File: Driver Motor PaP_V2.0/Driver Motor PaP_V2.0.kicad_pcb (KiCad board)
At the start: 2 copper layers, 70 x 60 mm, 31 parts, among them J1 Conn_01x02, J2 Conn_01x02, J3 Conn_01x04, J4 Conn_01x04, J5 Conn_01x01, J6 Conn_01x02, J7 Conn_01x02, J8 Conn_01x01, Q1 BC547, U1 LM358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

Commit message: Finalizado el ruteo. Revisar nuevamente
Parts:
- C4: footprint Capacitor_THT:CP_Radial_D10.0mm_P2.50mm -> Capacitor_THT:CP_Radial_D6.3mm_P2.50mm
- moved J5 21.8 mm to (140.5, 62.8)
- moved J3 18.9 mm to (90.0, 53.8)
- moved JP3 13.9 mm to (125.8, 87.8), turned to 0 degrees
- moved JP1 13.0 mm to (114.0, 87.8), turned to 0 degrees
- moved R2 9.53 mm to (117.0, 71.8), turned to 90 degrees
- moved R1 8.55 mm to (78.8, 76.0), turned to 90 degrees
- moved U3 8.04 mm to (125.8, 76.2), turned to 90 degrees
- moved C3 7.88 mm to (125.8, 64.5), turned to 0 degrees
- moved R3 7.25 mm to (123.0, 81.8), turned to 180 degrees
- moved JP5 5.94 mm to (103.5, 63.8)
- moved U2 5.50 mm to (133.2, 93.8)
- moved JP4 4.67 mm to (106.0, 75.2)
- moved JP2 4.09 mm to (120.0, 87.8)
- moved C2 3.26 mm to (133.5, 82.2), turned to 0 degrees
- moved J1 3.25 mm to (80.5, 89.5)
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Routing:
- net VCC: track 0.06 -> 130.9 mm
- net Net-(A1-Pad10): track 0.00 -> 40.3 mm
- net Net-(JP6-Pad2): track 0.00 -> 35.5 mm
- net Net-(A1-Pad11): track 0.00 -> 33.4 mm
- net Net-(J3-Pad4): track 0.00 -> 22.6 mm
- net Net-(JP2-Pad1): track 0.00 -> 20.9 mm
- net Net-(A1-Pad12): track 0.41 -> 20.3 mm
- net Net-(J4-Pad4): track 0.00 -> 19.0 mm
- net Net-(A1-Pad16): track 0.00 -> 18.0 mm
- net Net-(A1-Pad15): track 0.00 -> 16.1 mm
- net Net-(J4-Pad3): track 0.23 -> 16.3 mm
- net Net-(J5-Pad1): track 0.00 -> 14.6 mm
- net Net-(J4-Pad2): track 0.00 -> 11.7 mm
- net Net-(J3-Pad3): track 0.23 -> 11.9 mm
- net Net-(A1-Pad9): track 0.01 -> 11.0 mm
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- added copper zone on B.Cu, net GND
- added copper zone on F.Cu, net GND
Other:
- board text added: "Ancho de pista : 0,5 mm y 1.2 mm"
- board text added: "Autor: Esp. Ing. Luis Mariano Campos"
- board text added: "Diseño Argentino"
- board text added: "Distancia a borde: 0,5 mm"
- board text added: "Doble Faz"
- board text added: "Driver Motor PaP"
- board text added: "Facultad de Ingeniería - U.B.A."
- board text added: "Fault"
- board text added: "Grillas 0,25 mm"
- board text added: "M0"
- board text added: "M1"
- board text added: "M2"
- board text added: "Margen General: 0,5 mm"
- board text added: "Mínimos:"
- board text added: "PCB espesor: 1,6 mm"
- board text added: "Proyecto Final - CESE 8va Cohorte 2019"
- board text added: "Sherpa - v2.0"
- board text added: "Terminacioń HASL."
- board text added: "Vmotor"
- board text added: "ciaa"
- board text added: "dir"
- board text added: "enable"
- board text added: "gnd"
- board text added: "phase A"
- board text added: "phase B"
- board text added: "st-in"
- board text added: "st-out"
- board text added: "stp"
- board text added: "vcc"

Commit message: PCB FInalizadoy con BOM, realizar una última verificación
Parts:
- moved D1 0.25 mm to (80.2, 81.5)
- moved J1 0.25 mm to (80.8, 89.5)
- moved J3 0.25 mm to (90.0, 54.0)
- moved J4 0.25 mm to (140.8, 70.1)
- moved J6 0.25 mm to (92.0, 105.5)
- moved J7 0.25 mm to (100.3, 105.5)
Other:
- board text added: "ena"
- board text removed: "enable"

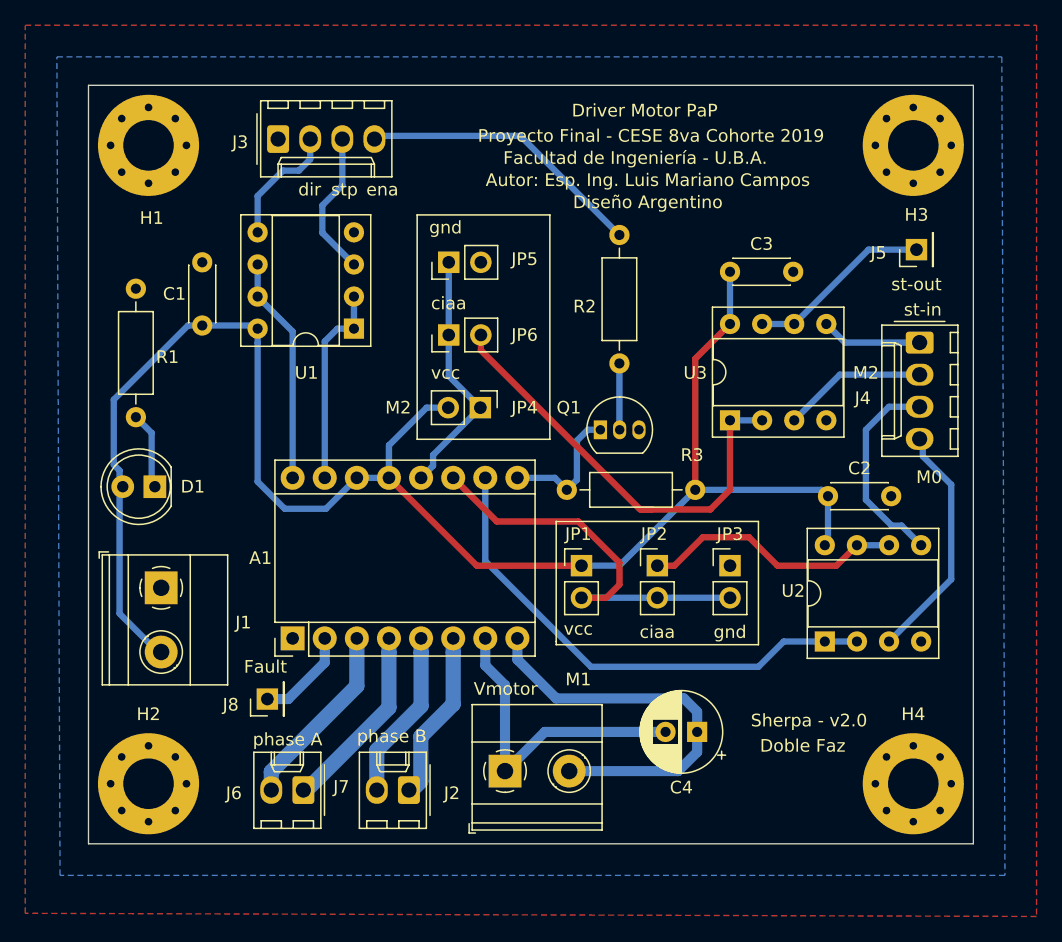
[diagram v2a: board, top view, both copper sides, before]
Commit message: Cambiando y creando nuevo Footprints y modelos 3D
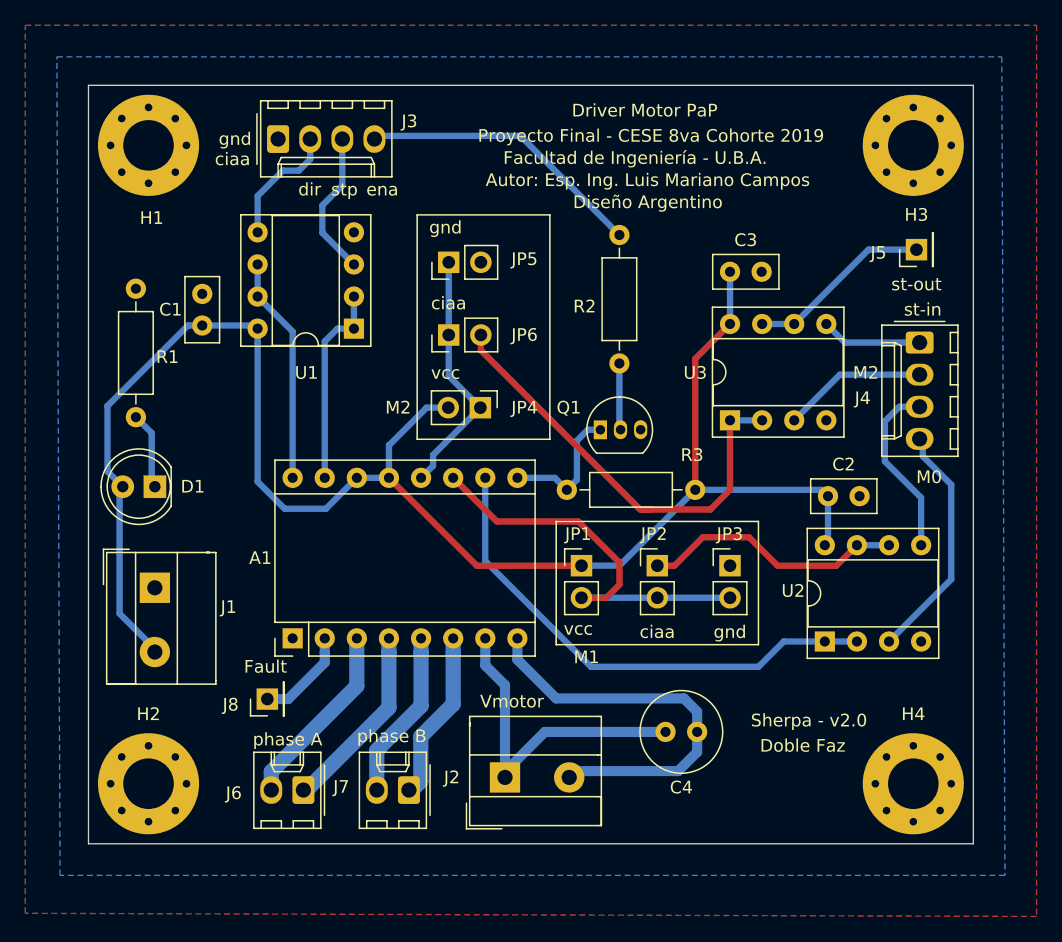
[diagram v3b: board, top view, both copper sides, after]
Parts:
- C1, C2, C3: footprint Capacitor_THT:C_Disc_D4.3mm_W1.9mm_P5.00mm -> Capacitor_THT:C_Disc_D5.0mm_W2.5mm_P2.50mm
- C4: footprint Capacitor_THT:CP_Radial_D6.3mm_P2.50mm -> Capacitor_THT:C_Radial_D6.3mm_H11.0mm_P2.50mm
- J1, J2: footprint TerminalBlock_Phoenix:TerminalBlock_Phoenix_MKDS-1,5-2-5.08_1x02_P5.08mm_Horizontal -> Terminal Degson:dg126
- moved J1 0.50 mm to (80.2, 89.5)
- moved J2 0.50 mm to (108.0, 104.5)
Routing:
- net Net-(J4-Pad3): track 16.7 -> 14.5 mm
- net VCC: track 130.9 -> 131.4 mm
